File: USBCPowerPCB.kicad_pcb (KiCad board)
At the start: 2 copper layers, 65.2 x 65.2 mm, 108 parts, among them IC2 TPS56A37RPAR, J1 USB_C_Receptacle_PowerOnly_6P, J10 GND_BANANA_OUT, J2 CC, J3 12V_OUT, J4 5V_ISO, J5 5V_OUT, J6 12V_OUT_PIN, J7 5V_ISO_PIN, J8 5V_OUT_PIN, J9 12V_BANANA_OUT, Q1 IRF9358TRPBF, Q2 BSL308PEH6327XTSA1, U1 TVS2200DRV, U2 CYPD3177-24LQXQT, U3 TPS562231DRLR, U4 TPS2116DRL, U5 TBA2-2411

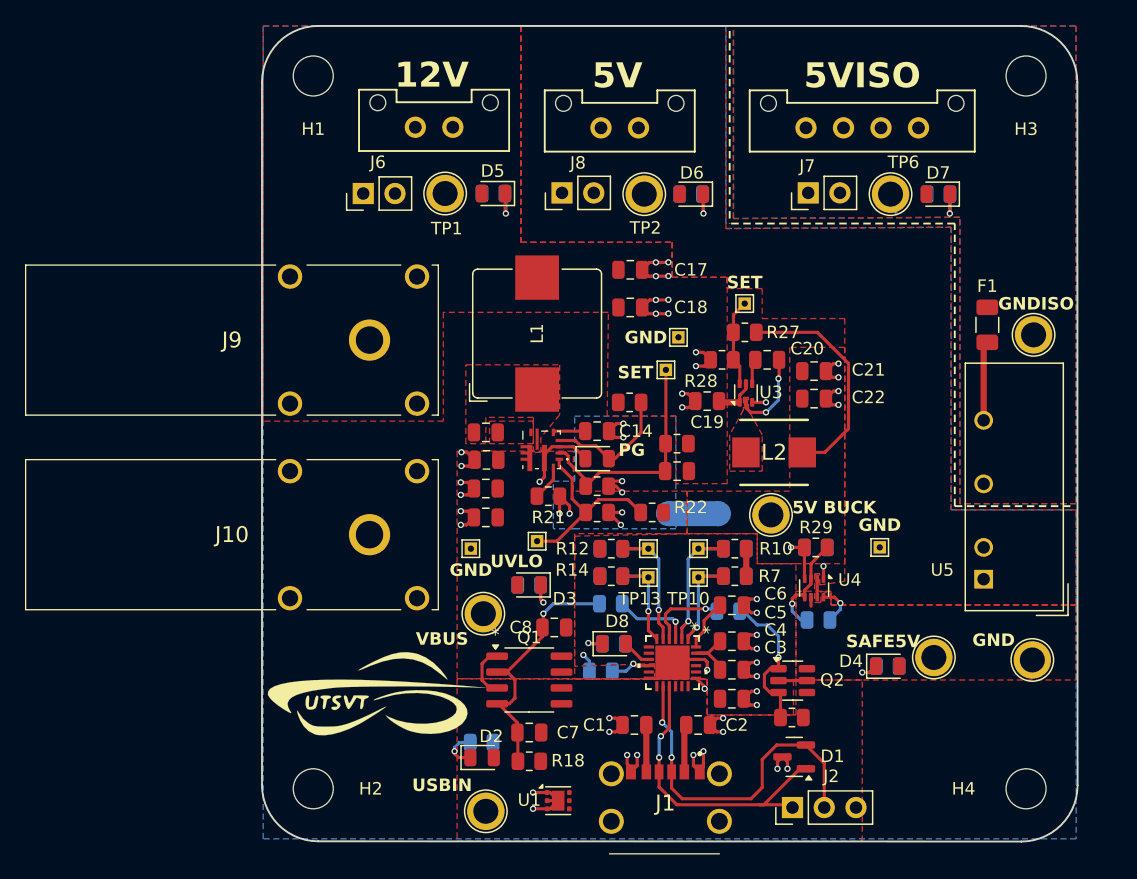
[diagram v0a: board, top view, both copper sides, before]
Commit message: made some changes to address review comments, still need to fix DRC fully and add UTSVT & Hallock silkscreen
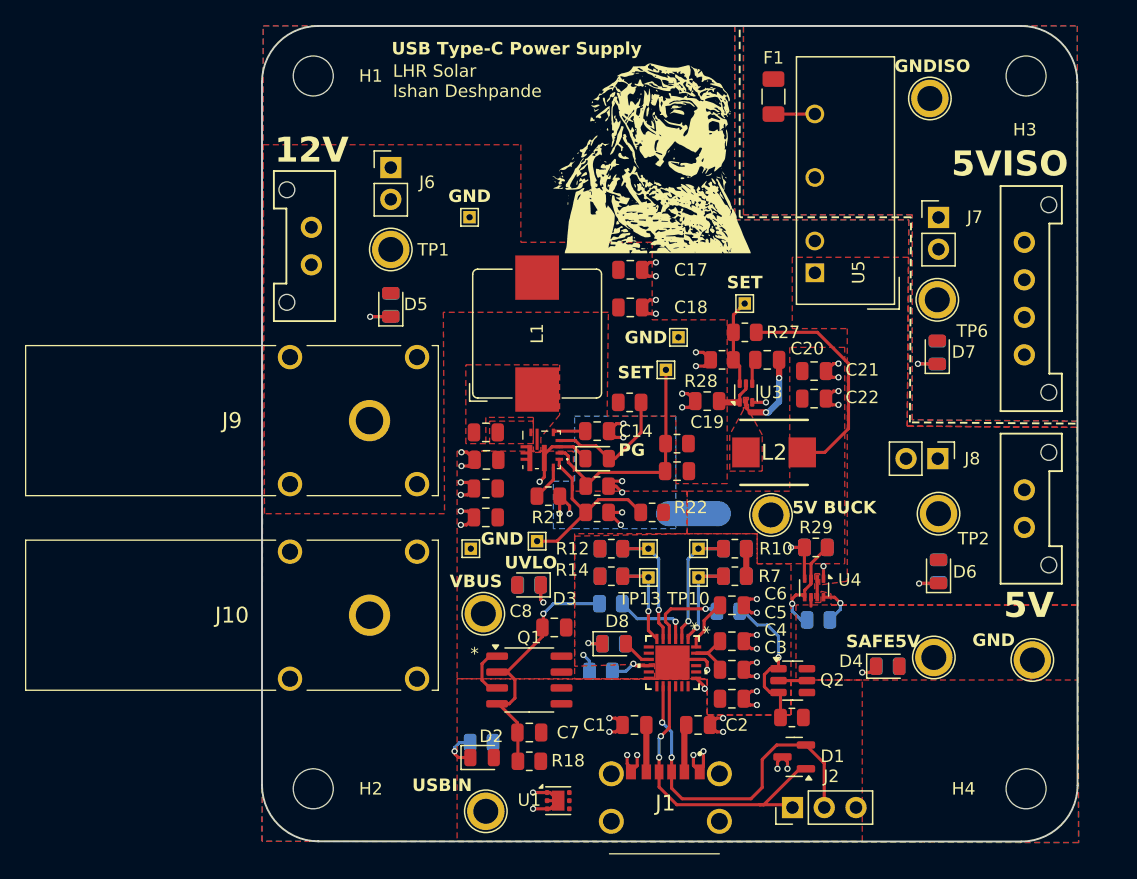
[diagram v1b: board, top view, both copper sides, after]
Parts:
- removed the G*** at (118.9, 133.9)
- removed the G*** at (117.8, 130.6)
- G***: moved to F.Cu
- moved J5 44.5 mm to (171.0, 117.5), turned to -90 degrees
- moved TP17 42.1 mm to (126.6, 95.7)
- moved J8 36.8 mm to (164.0, 115.0), turned to -90 degrees
- moved D6 36.1 mm to (164.1, 124.0), turned to 90 degrees
- moved R5 36.1 mm to (164.1, 124.0), turned to -90 degrees
- moved TP2 34.7 mm to (164.1, 119.4), turned to -90 degrees
- moved U5 28.0 mm to (154.2, 100.1)
- moved F1 25.0 mm to (150.9, 86.0)
- moved TP8 20.6 mm to (163.4, 86.2), turned to -90 degrees
- moved J4 19.7 mm to (171.0, 97.7), turned to -90 degrees
- moved G*** 18.6 mm to (143.5, 89.2), turned to 0 degrees
- moved J3 13.8 mm to (114.0, 99.5), turned to 90 degrees
- moved R6 12.7 mm to (164.0, 106.5), turned to -90 degrees
- moved D7 12.7 mm to (164.0, 106.5), turned to 90 degrees
- moved D5 12.1 mm to (120.3, 102.7), turned to 90 degrees
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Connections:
- J4 pad 2: unconnected-(J4-Pin_2-Pad2) -> GNDPWR
- J4 pad 4: GNDPWR -> unconnected-(J4-Pin_4-Pad4)
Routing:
- net GND: track 69.7 -> 65.7 mm, vias 47 -> 43
- net Net-(U5-+Vout): track 6.36 -> 3.31 mm
- net /5V_ISO: track 1.54 -> 0.00 mm
- added copper zone on F.Cu, net GND

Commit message: fixed clearance violations and made board 3mm shorter
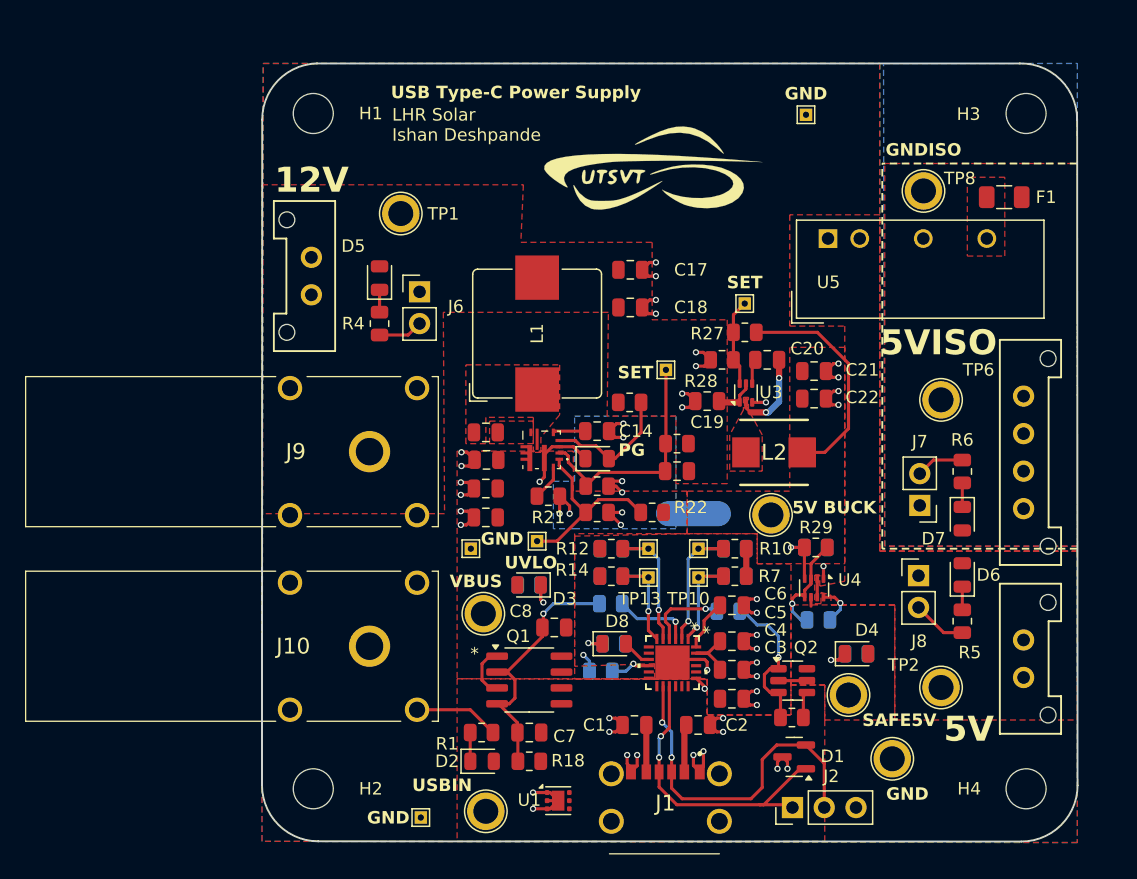
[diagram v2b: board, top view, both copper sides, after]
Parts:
- added G***: LOGO, UTSVT_Special:UTSVT_Logo_Symbol, F.Cu at (141.0, 91.9)
- added G***: LOGO, UTSVT_Special:Hallock_Image_Tiny, B.Cu at (128.2, 92.3)
- G***: moved to B.Cu
- R1, R4, R5, R6: moved to F.Cu
- moved TP5 43.6 mm to (122.7, 143.7)
- moved TP17 28.1 mm to (153.5, 87.5)
- moved J7 23.1 mm to (162.6, 118.7), turned to 180 degrees
- moved F1 20.1 mm to (169.3, 94.1), turned to 0 degrees
- moved TP2 13.9 mm to (164.3, 133.3)
- moved TP19 13.7 mm to (160.4, 139.0)
- moved D7 13.4 mm to (166.0, 119.8), turned to -90 degrees
- moved J4 12.3 mm to (170.9, 110.0)
- moved J5 12.0 mm to (170.9, 129.5)
- moved J6 10.2 mm to (122.6, 101.7)
- moved R6 9.71 mm to (166.0, 116.0)
- moved J8 9.49 mm to (162.5, 124.4), turned to 0 degrees
- moved TP6 8.01 mm to (164.3, 110.3), turned to -90 degrees
- moved TP7 7.46 mm to (156.9, 133.9)
- moved TP8 7.41 mm to (162.9, 93.6)
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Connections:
- net Net-(U5-+Vout) renamed /5V ORring and Isolator/5V_ISO_RAW
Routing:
- net GND: track 65.7 -> 79.3 mm
- net GNDPWR: track 0.00 -> 3.85 mm
- net /5V ORring and Isolator/5V_ISO_RAW: track 3.31 -> 0.00 mm
- net /VBUS_USBIN: track 7.56 -> 9.47 mm
- net Net-(D5-K): track 3.32 -> 1.79 mm, vias 1 -> 0
- net Net-(Q1A-S): track 4.46 -> 3.04 mm
- net Net-(D6-K): track 3.14 -> 1.85 mm, vias 1 -> 0
- net Net-(D7-K): track 3.11 -> 1.92 mm, vias 1 -> 0
- net Net-(D2-K): track 3.30 -> 2.31 mm, vias 1 -> 0
- net /CC1: track 24.6 -> 23.8 mm
- net /12V Buck Converter/FB: track 18.8 -> 18.0 mm
- net Net-(Q2A-G): track 12.2 -> 11.7 mm
- added copper zone on F.Cu, net /5V ORring and Isolator/5V_ISO_RAW
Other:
- board size 65.2 x 65.2 mm -> 65.2 x 62.2 mm

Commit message: cleaning up stuff
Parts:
- moved TP16 8.24 mm to (140.8, 116.0)
- moved R24 0.83 mm to (144.0, 113.8)
- moved C16 0.82 mm to (144.0, 116.0)
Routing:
- net /12V Buck Converter/FB: track 18.0 -> 7.72 mm
- net /VBUS_USBIN: track 9.47 -> 2.12 mm

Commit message: critical updates
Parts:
- added G***: LOGO, UTSVT_Special:wolf_front, B.Cu at (156.4, 88.7)
- moved G*** 3.62 mm to (143.8, 94.2)
- moved TP17 2.50 mm to (151.0, 87.5)
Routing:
- net /12V Buck Converter/FB: track 7.72 -> 13.1 mm

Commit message: addressed some review comments from my 🐐 champers fu
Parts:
- removed TP10: VBUS_MIN_TP, TestPoint:TestPoint_THTPad_1.0x1.0mm_Drill0.5mm
- removed TP11: VBUS_MAX_TP, TestPoint:TestPoint_THTPad_1.0x1.0mm_Drill0.5mm
- removed TP12: ISNK_COARSE_TP, TestPoint:TestPoint_THTPad_1.0x1.0mm_Drill0.5mm
- removed TP13: ISNK_FINE_TP, TestPoint:TestPoint_THTPad_1.0x1.0mm_Drill0.5mm
- LOGO1: renamed from G***; value LOGO -> UTSVT
- LOGO2: renamed from G***; value LOGO -> Hallock; moved to F.Cu
- LOGO3: renamed from G***; value LOGO -> Troll
- LOGO4: renamed from G***; value LOGO -> Wolf
- R11, R13, R15, R8: moved to F.Cu
- R4: value 5.1k -> 10k
- moved LOGO2 27.6 mm to (155.8, 92.3), turned to 0 degrees
- moved F1 19.7 mm to (173.8, 113.3)
- moved U5 19.7 mm to (159.7, 116.6)
- moved TP8 19.6 mm to (167.3, 112.7)
- moved LOGO4 16.0 mm to (159.2, 104.5)
- moved R6 12.5 mm to (169.1, 103.9)
- moved D7 12.5 mm to (169.1, 107.7)
- moved J7 12.5 mm to (165.7, 106.6)
- moved J4 12.5 mm to (173.9, 97.9)
- moved TP6 12.5 mm to (167.3, 98.2)
- moved LOGO3 12.5 mm to (153.4, 90.2)
- moved NT1 12.3 mm to (134.2, 112.8), turned to 180 degrees
- moved TP9 11.7 mm to (159.1, 111.3), turned to 180 degrees
- moved D6 3.64 mm to (169.1, 126.2)
- moved J8 3.64 mm to (165.6, 126.3)
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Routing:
- net /5V_BUCK: track 26.5 -> 8.40 mm
- net +3.3V: track 8.32 -> 12.3 mm
- net Net-(D3-K): track 2.98 -> 0.03 mm
- net Net-(D4-K): track 2.64 -> 0.03 mm
- net /Power Delivery Controller/ISNK_COARSE: track 11.8 -> 9.59 mm, vias 1 -> 0
- net /5V ORring and Isolator/MUX_SEL: track 4.62 -> 2.48 mm
- net /Power Delivery Controller/ISNK_FINE: track 9.09 -> 7.19 mm, vias 1 -> 0
- net /Power Delivery Controller/VBUS_MAX: track 11.8 -> 9.96 mm, vias 1 -> 0
- net /Power Delivery Controller/VBUS_MIN: track 8.84 -> 7.54 mm, vias 1 -> 0
- net GND: track 79.3 -> 79.9 mm, vias 43 -> 46
- net /Power Delivery Controller/VBUS_FET_EN: track 6.23 -> 6.83 mm
- removed copper zone on F.Cu, net +3.3V
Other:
- board size 65.2 x 62.2 mm -> 67.9 x 62.5 mm

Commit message: ready for review 👍🏾
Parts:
- R7: moved to B.Cu
- moved R9 1.49 mm to (137.8, 133.3), turned to -90 degrees
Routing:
- net +3.3V: track 12.3 -> 28.0 mm, vias 1 -> 4
- net GNDA: track 10.9 -> 4.61 mm
- net GND: track 79.9 -> 76.0 mm, vias 46 -> 48
- net Net-(D8-K): track 2.30 -> 0.00 mm
- net /Power Delivery Controller/SAFE_5V_EN: track 6.32 -> 7.38 mm
- net /Power Delivery Controller/VBUS_FET_EN: track 6.83 -> 7.51 mm
- net /Power Delivery Controller/VBUS_MIN: vias 0 -> 1

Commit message: uncurse the cursed board
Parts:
- moved D4 2.87 mm to (158.5, 127.9), turned to 180 degrees
- moved R3 2.87 mm to (158.5, 127.9), turned to 0 degrees
- moved C8 1.92 mm to (131.7, 127.5), turned to 0 degrees
- moved D3 0.34 mm to (131.7, 125.1)
- moved R2 0.34 mm to (131.7, 125.1)
- moved TP16 0.30 mm to (141.1, 116.0)
- moved D8 0.24 mm to (137.9, 129.8)
- moved R20 0.24 mm to (137.9, 129.8)
- turned R26 to 180 degrees
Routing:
- net Net-(Q1A-G): track 21.0 -> 22.2 mm
